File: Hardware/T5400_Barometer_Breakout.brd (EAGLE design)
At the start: 25.4 x 14 mm, 11 parts, among them U1 T5400

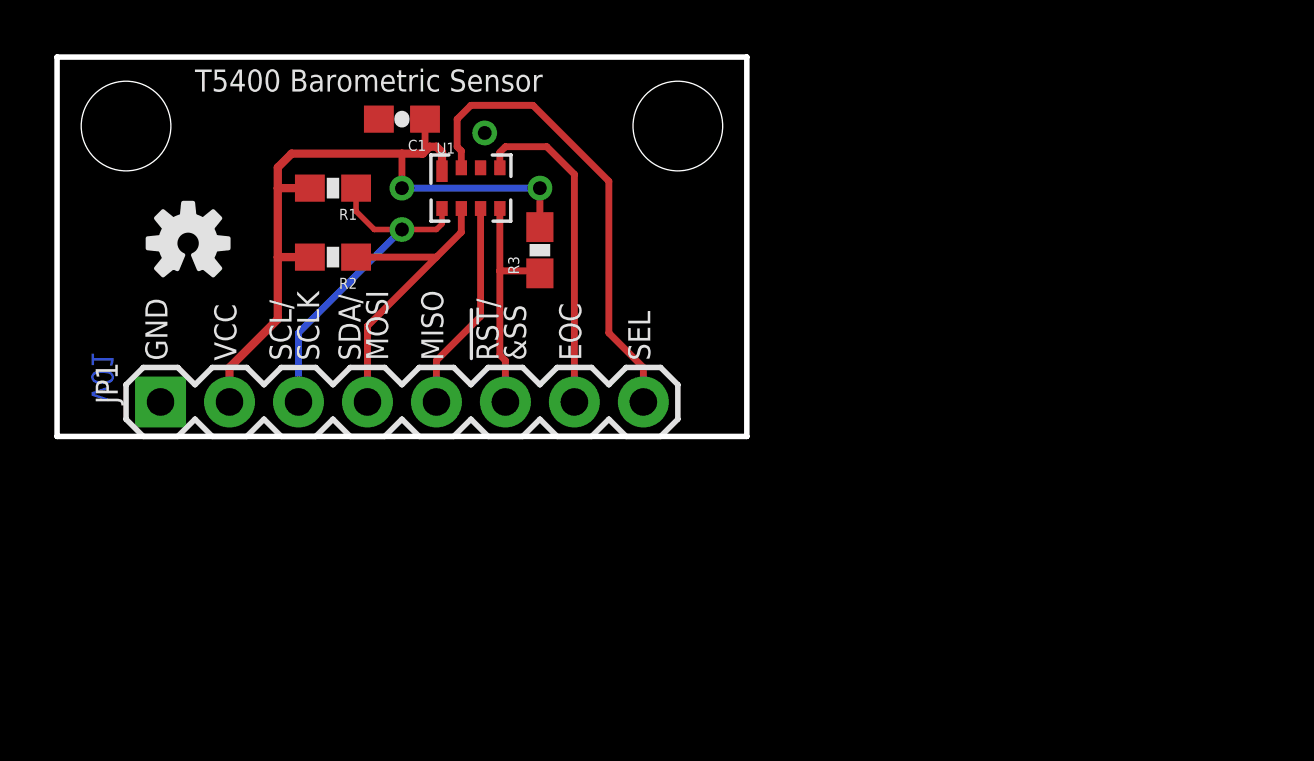
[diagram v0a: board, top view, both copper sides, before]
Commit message: READY for proto
Corrected boards per meeting agenda.  Also changed names
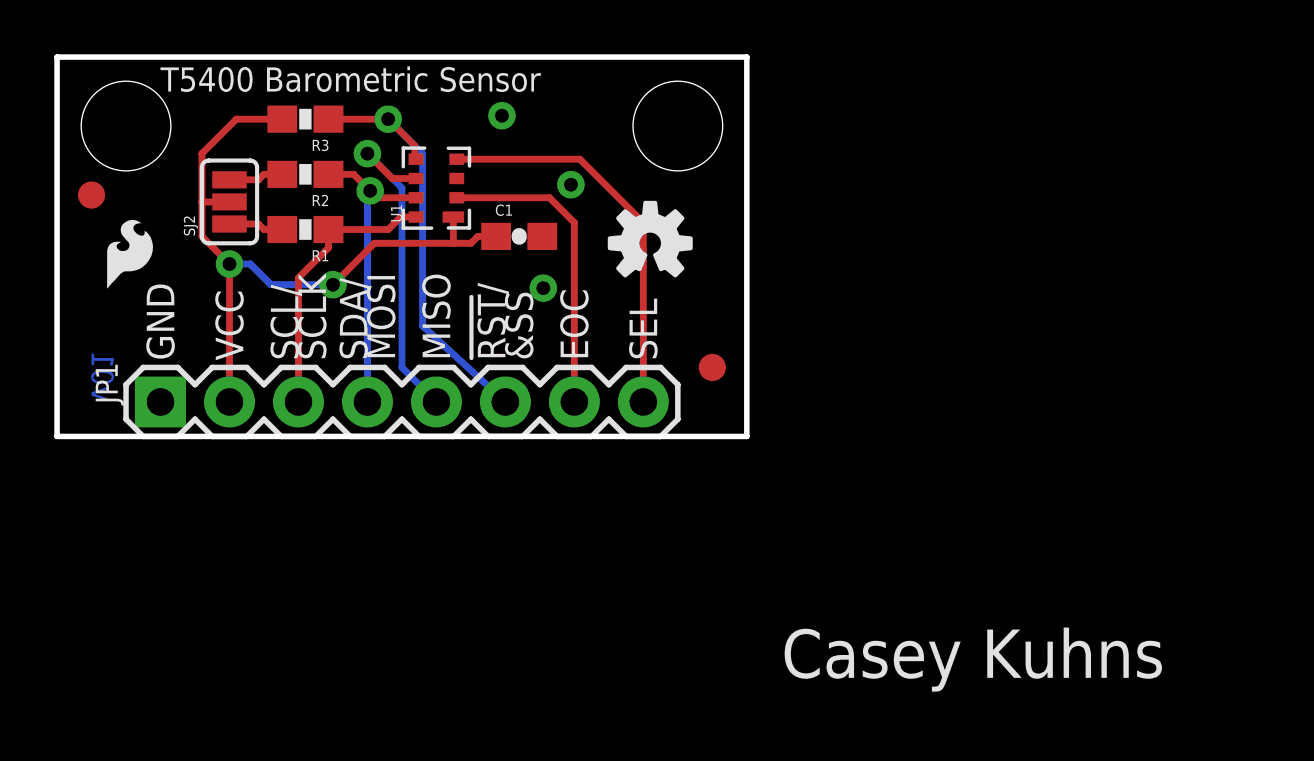
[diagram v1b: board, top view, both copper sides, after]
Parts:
- added FID1, FID2: FIDUCIAL1X2, SparkFun-Aesthetics:FIDUCIAL-1X2
- added LOGO3: SFE_LOGO_FLAME.1_INCH, SparkFun-Aesthetics:SFE_LOGO_FLAME_.1
- added SJ2: (no value), SparkFun-Passives:SJ_3_PASTE1&2&3
- moved LOGO2 17.0 mm to (21.8, 7.11)
- moved R3 9.89 mm to (9.14, 11.7), turned to 180 degrees
- moved C1 6.11 mm to (17.0, 7.37), turned to 0 degrees
- moved R2 3.21 mm to (9.14, 9.65)
- moved R1 1.83 mm to (9.14, 7.62)
- moved U1 1.27 mm to (14.0, 9.14), turned to 90 degrees
- moved LOGO1 1.14 mm to (22.4, 6.10)
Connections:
- new net N$1: R2.2, SJ2.3
- new net N$2: R1.2, SJ2.1
- net EOC: now also JP1.8; no longer JP1.7
- net SEL: now also JP1.7; no longer JP1.8
- net VCC: now also SJ2.2; no longer R1.2, R2.2
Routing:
- net !RST!/&SS: track 8.72 -> 16.5 mm, vias 0 -> 1
- net SEL: track 17.5 -> 11.3 mm
- net MISO: track 7.80 -> 12.4 mm, vias 0 -> 1
- net SCL/SCLK: track 12.9 -> 10.2 mm, vias 1 -> 0
- net EOC: track 12.2 -> 14.4 mm
- net VCC: track 28.0 -> 25.9 mm
- net N$2: track 0.00 -> 2.03 mm
- net N$1: track 0.00 -> 2.03 mm
- net SDA/MOSI: track 11.5 -> 11.6 mm, vias 0 -> 1
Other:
- board text added: "Casey Kuhns"

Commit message: removed fiducials
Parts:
- removed FID1, FID2: FIDUCIAL1X2, SparkFun-Aesthetics:FIDUCIAL-1X2
